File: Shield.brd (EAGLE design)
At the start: 99.1 x 68.6 mm, 71 parts

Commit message: Added Gerber Files
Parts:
- moved 0.1UF-4 1.27 mm to (50.3, 40.1)
- moved 1UF-2 1.27 mm to (38.9, 31.8)
- moved 2.2K 1.27 mm to (87.6, 53.1)
- moved 2.2K-2 1.27 mm to (87.6, 55.6)
- moved 2.2K-3 1.27 mm to (87.6, 48.0)
- moved 2.2K-4 1.27 mm to (87.6, 50.5)
- moved 6.8UF 1.27 mm to (58.2, 36.1)
- moved BATT 1.27 mm to (63.5, 45.7)
- moved LED1 1.27 mm to (16.8, 63.8)
- moved LED2 1.27 mm to (21.8, 63.8)
- moved OPA1TERM 1.27 mm to (5.08, 58.7)
- moved SDLVLS 1.27 mm to (38.1, 45.7)
- moved U$1 1.27 mm to (26.7, 36.8)
- moved Y1 1.27 mm to (71.6, 39.9)
- moved 0.1UF-5 1.27 mm to (4.32, 11.7)
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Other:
- outline, holes or cut-outs redrawn

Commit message: Beginning Board Revision 2
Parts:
- removed 6.8U-T: CES, LEMS:E2,5-5
- removed U$4: 2PHN, LEMS:2PH
- added 3.3VTERM, 5VTERM, GNDTERM: 3PHS, LEMS:SCREWTERMINAL-3.5MM-3_LOCK.007S
- added 4.5VJUMP, 5V_JUMP: 2PJN, LEMS:2PH
- added 6.8UF-T: CES, LEMS:E2,5-5
- added BMP085TERM: 6PHN, LEMS:6PH
- added OPAMPEXTRA1, OPAMPEXTRA2: 3PHN, LEMS:3PH
- added TN9POWTERM: 2PHS, LEMS:SCREWTERMINAL-3.5MM-2_LOCK
- 44.2K: value RESISTORT -> RESISTORN; device LEMS:0207/7 -> LEMS:0207/10
- moved BATT 57.9 mm to (7.11, 58.9)
- moved OPA1TERM 54.5 mm to (15.2, 5.08), turned to 0 degrees
- moved 0.1UF-5 36.9 mm to (34.0, 33.5), turned to 270 degrees
- moved 250K 33.9 mm to (40.6, 41.4)
- moved U$18 33.8 mm to (40.6, 33.8), turned to 180 degrees
- moved 4.7K 29.3 mm to (85.1, 35.6), turned to 0 degrees
- moved U$9 28.8 mm to (66.0, 33.0)
- moved 0.1UF 28.8 mm to (55.6, 34.0)
- moved 0.1UF-2 28.8 mm to (55.6, 39.4)
- moved 100UF-2 28.8 mm to (60.5, 39.4)
- moved 100UF 27.9 mm to (59.2, 34.0)
- moved S1 24.4 mm to (17.0, 39.9)
- moved U$11 22.2 mm to (75.4, 19.1), turned to 180 degrees
- moved 1 21.7 mm to (37.1, 26.2)
- moved 10UF 21.7 mm to (69.6, 23.6), turned to 180 degrees
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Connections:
- new net 5VOUT: 250K.2, 5V_JUMP.1, 6.8UF-T.+, U$18.1, U$18.7, U$18.8
- new net EOC: BMP085TERM.4
- new net XCLR: BMP085TERM.3
- net 3.3V: now also BMP085TERM.6
- net 3.3V_SCL: now also BMP085TERM.2
- net 3.3V_SDA: now also BMP085TERM.1
- net 4.5V: now also 4.5VJUMP.1; no longer U$4.1, U$4.2
- net 5V: now also 5VTERM.1, 5VTERM.2, 5VTERM.3, 5V_JUMP.2, TN9POWTERM.2; no longer 250K.2, 6.8U-T.+, U$18.1, U$18.7, U$18.8
- net AREF: now also 4.5VJUMP.2
- net GND: now also BMP085TERM.5, GNDTERM.1, GNDTERM.2, GNDTERM.3, TN9POWTERM.1
- net MEGA3.3V: now also 3.3VTERM.1, 3.3VTERM.2, 3.3VTERM.3
- net N$7: now also 6.8UF-T.-; no longer 6.8U-T.-
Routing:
- net GND: track 482.6 -> 138.3 mm, vias 1 -> 0
- net 5V: track 252.7 -> 80.5 mm, vias 1 -> 0
- net 3.3V: track 151.2 -> 14.1 mm, vias 2 -> 0
- net 3.3V_SCL: track 28.4 -> 103.6 mm
- net 3.3V_SDA: track 21.2 -> 95.1 mm
- net 4.5V: track 83.5 -> 37.5 mm
- net D38: track 89.3 -> 53.8 mm, vias 2 -> 0
- net N$8: track 29.4 -> 0.00 mm
- net SS_SOFT: track 26.5 -> 0.00 mm
- net CH2: track 23.8 -> 46.7 mm, vias 0 -> 1
- net VBAT: track 22.3 -> 0.00 mm
- net SD_CSIN: track 20.4 -> 0.00 mm
- net MOSI_SOFT: track 20.2 -> 0.00 mm
- net MEGA3.3V: track 0.00 -> 19.9 mm
- net MISO_SOFT: track 17.0 -> 0.00 mm
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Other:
- board text added: "50"
- board text added: "52"
- board text added: "A15"
- board text added: "A3"
- board text removed: "+"
- board text removed: "-"
- board text removed: "3.3I2C"
- board text removed: "4.5V"
- board text removed: "G"
- board text removed: "Licor"
- board text removed: "OFF"
- board text removed: "POWER IN"
- board text removed: "TN9"

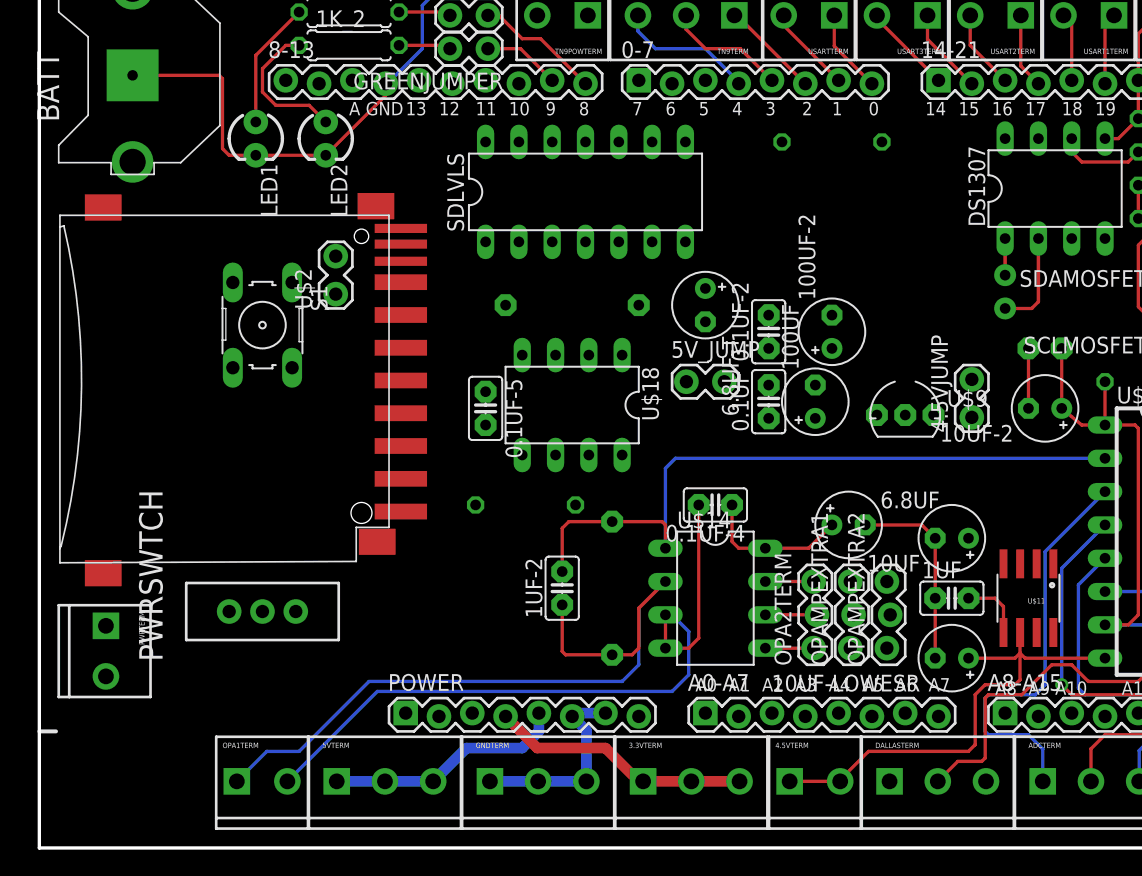
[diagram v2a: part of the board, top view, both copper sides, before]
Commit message: Still need to finalize power components
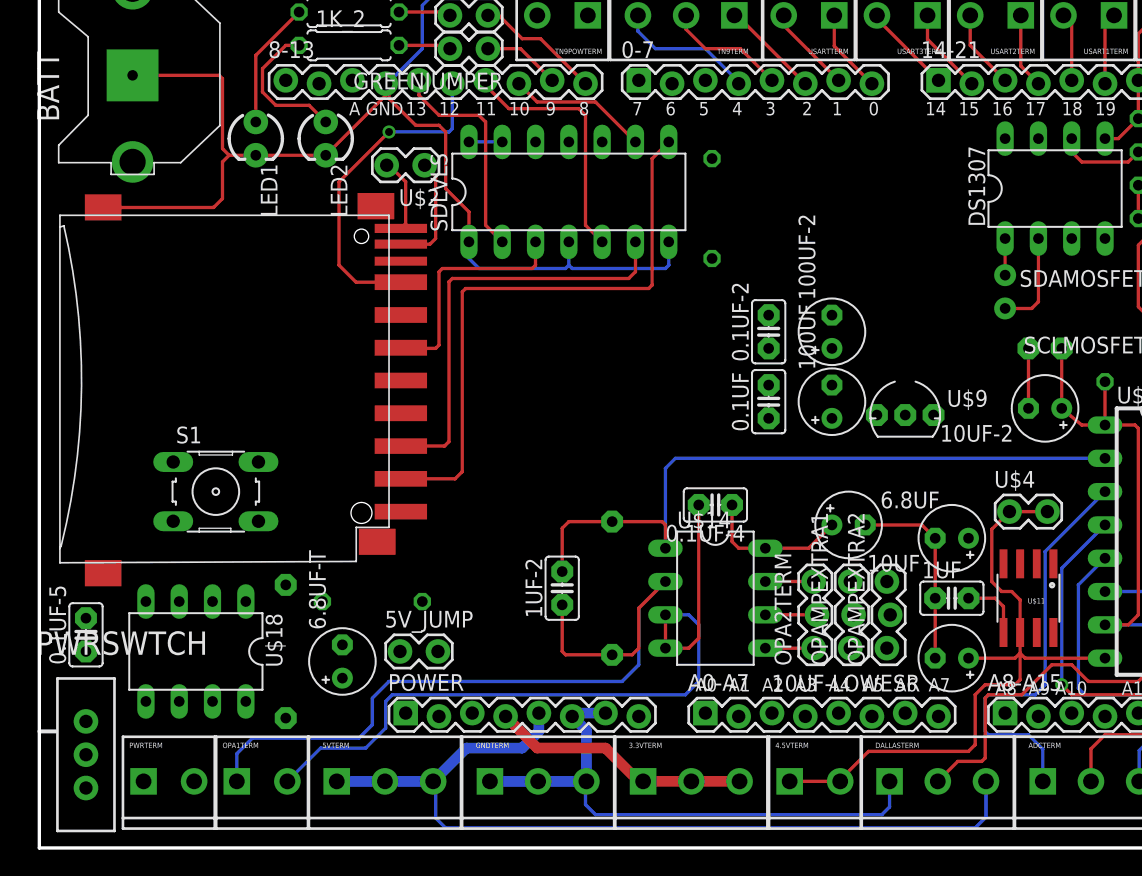
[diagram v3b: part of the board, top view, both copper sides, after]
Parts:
- removed 4.5VJUMP: 2PJN, LEMS:2PH
- added U$4: 2PHN, LEMS:2PH
- moved 6.8UF-T 38.8 mm to (23.1, 14.2), turned to 90 degrees
- moved 0.1UF-5 35.0 mm to (3.56, 16.3), turned to 90 degrees
- moved U$18 34.3 mm to (11.9, 15.0)
- moved 250K 34.3 mm to (18.8, 15.0), turned to 270 degrees
- moved 5V_JUMP 30.0 mm to (29.0, 15.0)
- moved PWRSWTCH 17.3 mm to (3.56, 7.11), turned to 0 degrees
- moved 1 13.8 mm to (25.4, 18.8), turned to 180 degrees
- moved S1 13.2 mm to (13.5, 27.2), turned to 0 degrees
- moved PWRTERM 12.1 mm to (8.13, 5.08), turned to 0 degrees
- moved 10K 10.5 mm to (51.3, 48.8), turned to 90 degrees
- moved U$2 9.94 mm to (27.9, 52.1), turned to 180 degrees
- moved 100UF 1.27 mm to (60.5, 34.0)
- moved SDLVLS 1.27 mm to (40.4, 50.0)
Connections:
- net 4.5V: now also U$4.1, U$4.2; no longer 4.5VJUMP.1
- net AREF: no longer 4.5VJUMP.2
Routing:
- net GND: track 138.3 -> 218.5 mm
- net 5V: track 80.5 -> 128.8 mm
- net SD_CSIN: track 0.00 -> 44.8 mm
- net SD_DATAIN: track 0.00 -> 32.8 mm
- net MISO_SOFT: track 0.00 -> 25.3 mm, vias 0 -> 1
- net MOSI_SOFT: track 0.00 -> 19.1 mm
- net SD_SCKIN: track 0.00 -> 18.0 mm
- net SCK_SOFT: track 0.00 -> 16.7 mm
- net 4.5V: track 37.5 -> 51.5 mm
- net SS_SOFT: track 0.00 -> 10.7 mm
- net SD_CD: track 0.00 -> 8.77 mm
- net SD_WP: track 0.00 -> 5.68 mm
- net 3.3V: track 14.1 -> 16.7 mm
- net LIOP-: track 57.2 -> 59.6 mm

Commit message: Complete Prototype #2
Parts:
- removed S1: (no value), LEMS:B3F-10XX
- removed U$4: 2PHN, LEMS:2PH
- moved 100UF 31.3 mm to (31.2, 22.9), turned to 180 degrees
- moved U$9 31.0 mm to (35.3, 28.7)
- moved 0.1UF 28.7 mm to (32.8, 16.8)
- moved 100UF-2 25.6 mm to (35.3, 34.5), turned to 180 degrees
- moved 0.1UF-2 20.3 mm to (35.3, 38.9), turned to 180 degrees
- moved 10K 2.59 mm to (50.8, 51.3)
- moved 10UF-2 1.27 mm to (76.7, 34.8)
- moved 1K 1.27 mm to (23.6, 65.0)
- moved 1K_2 1.27 mm to (23.6, 62.5)
- moved 2.2K 1.27 mm to (87.6, 54.4)
- moved 2.2K-2 1.27 mm to (87.6, 56.9)
- moved 2.2K-3 1.27 mm to (87.6, 49.3)
- moved 2.2K-4 1.27 mm to (87.6, 51.8)
- moved BATT 1.27 mm to (7.11, 60.2)
- moved LED1 1.27 mm to (16.5, 55.4)
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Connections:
- net N$8 renamed REG_IN
- net 4.5V: no longer U$4.1, U$4.2
- net GND: no longer S1.3, S1.4
- net RESET: no longer S1.1, S1.2
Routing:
- net GND: track 218.5 -> 487.6 mm
- net 3.3V: track 16.7 -> 218.9 mm, vias 0 -> 3
- net 5V: track 128.8 -> 319.6 mm
- net VBAT: track 0.00 -> 111.7 mm
- net 5VOUT: track 0.00 -> 23.7 mm
- net REG_IN: track 0.00 -> 14.9 mm
- net 4.5V: track 51.5 -> 37.5 mm
- net PWRN: track 0.00 -> 10.4 mm
- net N$6: track 0.00 -> 8.15 mm
- net SS_SOFT: track 10.7 -> 18.9 mm
- net N$7: track 0.00 -> 4.29 mm
- net MISO: track 25.6 -> 27.2 mm
- net MISO_SOFT: track 25.3 -> 26.2 mm
- net MOSI_SOFT: track 19.1 -> 19.9 mm
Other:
- board size 99.1 x 68.6 mm -> 99.1 x 71.1 mm
- board text added: "3.3V"
- board text added: "4.5V"
- board text added: "ACT"
- board text added: "CH1"
- board text added: "CH2"
- board text added: "CH3"
- board text added: "CLK"
- board text added: "DAT"
- board text added: "GROUND"
- board text added: "LI+"
- board text added: "LI-"
- board text added: "MISO"
- board text added: "MOSI"
- board text added: "ON"
- board text added: "RX0"
- board text added: "RX1"
- board text added: "RX2"
- board text added: "RX3"
- board text added: "SCK"
- board text added: "SCL3"
- board text added: "SCL5"
- board text added: "SDA3"
- board text added: "SDA5"
- board text added: "TEMP"
- board text added: "TX0"
- board text added: "TX1"
- board text added: "TX2"
- board text added: "TX3"
- board text added: "VIN+"
- board text added: "VIN-"
- board text removed: "A7"
- board text removed: "SPI"

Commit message: Started Revision 3
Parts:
- moved BMP085TERM 62.7 mm to (83.8, 39.9), turned to 180 degrees
- moved PWRSWTCH 38.5 mm to (36.1, 29.0), turned to 270 degrees
- moved OPA1TERM 35.1 mm to (50.3, 6.35)
- moved 100UF 34.2 mm to (60.5, 40.6)
- moved 100UF-2 32.1 mm to (62.0, 52.3)
- moved U$9 31.0 mm to (60.7, 46.5)
- moved 3.3VTERM 30.5 mm to (15.7, 6.35)
- moved 10UF-2 25.4 mm to (51.3, 33.5)
- moved 0.1UF-2 20.5 mm to (54.4, 46.5)
- moved 0.1UF-3 19.7 mm to (57.7, 34.3)
- moved U$11 18.3 mm to (65.3, 35.6)
- moved 5VTERM 16.3 mm to (39.1, 6.35)
- moved LED1 13.3 mm to (20.6, 68.1), turned to 180 degrees
- moved SCLMOSFET 9.48 mm to (88.9, 50.3)
- moved U$2 9.25 mm to (19.1, 55.9)
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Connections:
- net 5V: now also TN9POWTERM.1; no longer TN9POWTERM.2
- net GND: now also TN9POWTERM.2; no longer TN9POWTERM.1
- net VBAT: now also BATT.+2; no longer BATT.+1
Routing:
- net GND: track 487.6 -> 72.3 mm
- net 3.3V: track 218.9 -> 16.3 mm, vias 3 -> 0
- net 5V: track 319.6 -> 118.4 mm
- net 3.3V_SCL: track 103.6 -> 31.7 mm
- net 3.3V_SDA: track 95.1 -> 27.1 mm
- net LIOP-: track 59.6 -> 0.00 mm
- net CH0: track 53.2 -> 0.00 mm
- net SD_CSIN: track 44.3 -> 0.00 mm
- net 4.5V: track 37.5 -> 0.00 mm
- net SD_DATAIN: track 32.8 -> 0.00 mm
- net VBAT: track 111.7 -> 83.2 mm
- net MISO_SOFT: track 26.2 -> 0.00 mm, vias 1 -> 0
- net 5VOUT: track 23.7 -> 0.00 mm
- net MEGA3.3V: track 19.9 -> 0.00 mm
- net MOSI_SOFT: track 19.9 -> 0.00 mm
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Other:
- board text added: "20"
- board text added: "21"
- board text added: "22"
- board text added: "VCC"
- board text removed: "3.3V"
- board text removed: "32"
- board text removed: "34"
- board text removed: "36"
- board text removed: "GROUND"
- board text removed: "LI+"
- board text removed: "LI-"
- board text removed: "ON"
- board text removed: "VIN+"
- board text removed: "VIN-"

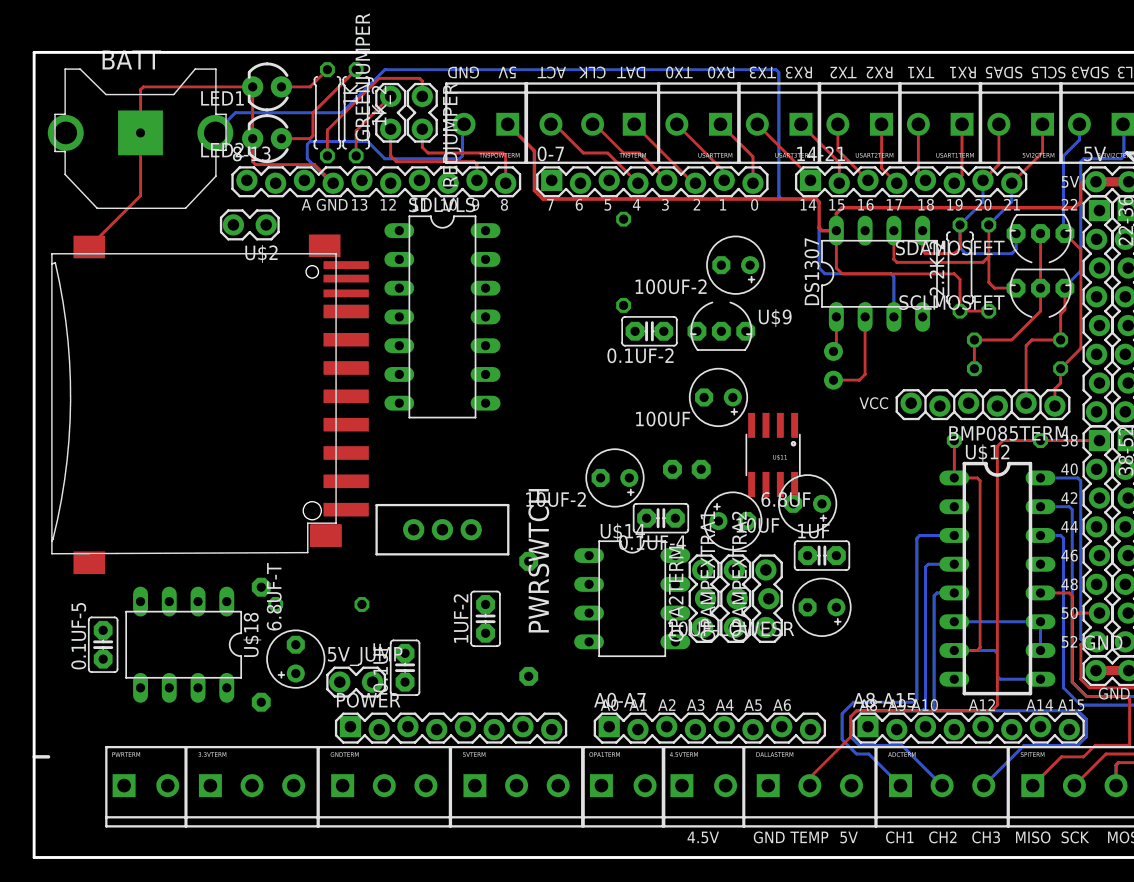
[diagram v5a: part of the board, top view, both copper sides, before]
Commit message: Added everything but power, charging, and various silkscreen
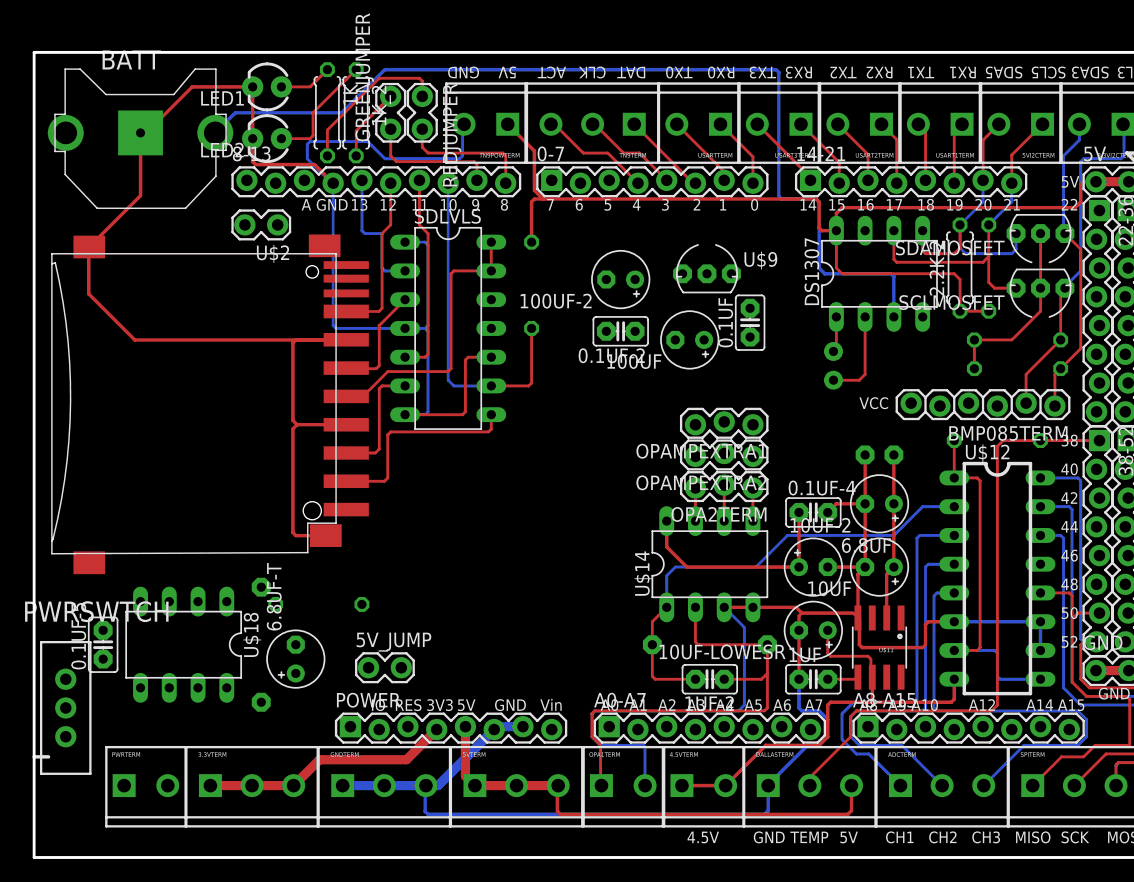
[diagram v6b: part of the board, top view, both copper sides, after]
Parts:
- moved 0.1UF 43.1 mm to (63.2, 47.2)
- moved PWRSWTCH 36.8 mm to (2.79, 13.2), turned to 0 degrees
- moved 10UF-2 23.5 mm to (74.7, 31.2)
- moved 1UF-2 20.5 mm to (59.7, 15.7), turned to 180 degrees
- moved U$11 19.4 mm to (74.7, 18.5)
- moved OPAMPEXTRA1 18.1 mm to (63.5, 38.4), turned to 180 degrees
- moved 0.1UF-3 17.1 mm to (74.7, 35.6)
- moved 44.2K 16.2 mm to (59.7, 18.8), turned to 0 degrees
- moved OPAMPEXTRA2 15.3 mm to (63.5, 35.6), turned to 180 degrees
- moved 0.1UF-4 13.5 mm to (68.8, 30.5), turned to 0 degrees
- moved OPA2TERM 13.2 mm to (63.5, 32.8), turned to 180 degrees
- moved 1UF 10.9 mm to (68.8, 15.7)
- moved 100UF-2 10.2 mm to (51.8, 51.1)
- moved 10UF 8.46 mm to (74.7, 25.7)
- moved 10K 8.38 mm to (43.9, 50.5), turned to 270 degrees
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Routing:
- net GND: track 72.3 -> 334.9 mm
- net 5V: track 118.4 -> 200.9 mm
- net LIOP-: track 0.00 -> 41.5 mm
- net CH0: track 0.00 -> 41.3 mm
- net 4.5V: track 0.00 -> 40.6 mm
- net SS_SOFT: track 0.00 -> 29.9 mm
- net 3.3V: track 16.3 -> 41.1 mm
- net MEGA3.3V: track 0.00 -> 22.0 mm
- net SD_CSIN: track 0.00 -> 18.2 mm
- net MOSI_SOFT: track 0.00 -> 17.8 mm
- net MISO_SOFT: track 0.00 -> 14.6 mm
- net SCK_SOFT: track 0.00 -> 11.5 mm
- net SD_DATAIN: track 0.00 -> 10.8 mm
- net SD_SCKIN: track 0.00 -> 9.83 mm
- net N$3: track 0.00 -> 3.18 mm
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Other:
- board text added: "3V3"
- board text added: "A7"
- board text added: "IO"
- board text added: "RES"
- board text added: "Vin"
